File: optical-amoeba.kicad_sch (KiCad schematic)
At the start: 5 parts, among them J1 Conn_01x08_Male, Q1 Q_Photo_NPN_CE

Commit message: Added PCB for full keyboard
 M .gitignore
A  OpticalSymbols_Library.kicad_sym
A  Optical_Parts.pretty/BlackPill_STLINK.kicad_mod
M  Optical_Parts.pretty/Everlight_IR_IR12-21C_TR8.kicad_mod
M  Optical_Parts.pretty/Everlight_PT_PT12-21C_TR8.kicad_mod
M  Optical_Parts.pretty/Gateron_Optical_Switch.kicad_mod
A  Optical_Parts.pretty/Gateron_Switch_Basic.kicad_mod
A  Optical_Parts.pretty/Switch_Cutout.kicad_mod
A  Optical_Parts.pretty/Switch_Cutout_1.25u.kicad_mod
A  Optical_Parts.pretty/Switch_Cutout_1.5u.kicad_mod
A  Optical_Parts.pretty/Switch_Cutout_1.75u.kicad_mod
M  README.md
A  keyboard-pcb/.gitignore
A  keyboard-pcb/fp-lib-table
A  keyboard-pcb/keyboard-pcb.kicad_pcb
A  keyboard-pcb/keyboard-pcb.kicad_prl
A  keyboard-pcb/keyboard-pcb.kicad_pro
A  keyboard-pcb/keyboard-pcb.kicad_sch
A  keyboard-pcb/placefp.py
A  keyboard-pcb/switch.kicad_sch
A  keyboard-pcb/sym-lib-table
M  optical-amoeba.kicad_pcb
M  optical-amoeba.kicad_sch
A  switch-cutout/.gitignore
A  switch-cutout/fp-lib-table
A  switch-cutout/switch-cutout.kicad_pcb
A  switch-cutout/switch-cutout.kicad_prl
A  switch-cutout/switch-cutout.kicad_pro
A  switch-cutout/switch-cutout.kicad_sch
A  sym-lib-table
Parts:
- Q1: footprint Optical_Parts:Everlight_PT_PT12-21B_TR8 -> Optical_Parts:Everlight_PT_PT12-21C_TR8
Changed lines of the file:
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@@
       (effects (font (size 1.27 1.27)) (justify left))
     )
-    (property "Footprint" "Optical_Parts:Everlight_PT_PT12-21B_TR8" (id 2) (at 125.73 80.01 0)
+    (property "Footprint" "Optical_Parts:Everlight_PT_PT12-21C_TR8" (id 2) (at 125.73 80.01 0)
       (effects (font (size 1.27 1.27)) hide)
     )
@@
     )
     (path "/548bb468-a13e-41e7-a6b9-f73eb3b9ea63"
-      (reference "Q1") (unit 1) (value "Q_Photo_NPN_CE") (footprint "Optical_Parts:Everlight_PT_PT12-21B_TR8")
+      (reference "Q1") (unit 1) (value "Q_Photo_NPN_CE") (footprint "Optical_Parts:Everlight_PT_PT12-21C_TR8")
     )
     (path "/23503685-6c48-4b6b-a5a1-d4b81440ce50"

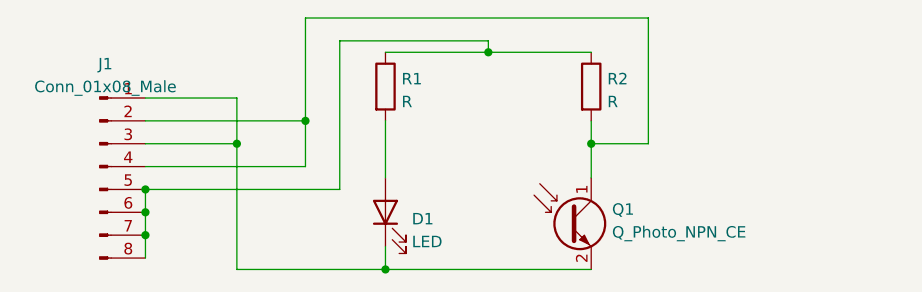
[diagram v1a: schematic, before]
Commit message: Added footprints
M  Optical_Parts.pretty/BlackPill_STLINK.kicad_mod
M  Optical_Parts.pretty/BlackPill_STLINK2.kicad_mod
M  Optical_Parts.pretty/Everlight_IR_IR12-21C_TR8.kicad_mod
M  Optical_Parts.pretty/Everlight_PT_PT12-21C_TR8.kicad_mod
M  Optical_Parts.pretty/Gateron_Optical_Switch.kicad_mod
M  Optical_Parts.pretty/MountingHole_2.2mm_M2_jlcpcb.kicad_mod
M  Optical_Parts.pretty/Switch_Cutout.kicad_mod
M  Optical_Parts.pretty/Switch_Cutout_1.25u.kicad_mod
M  Optical_Parts.pretty/Switch_Cutout_1.5u.kicad_mod
M  Optical_Parts.pretty/Switch_Cutout_1.75u.kicad_mod
M  README.md
M  optical-amoeba.kicad_pcb
M  optical-amoeba.kicad_prl
M  optical-amoeba.kicad_sch
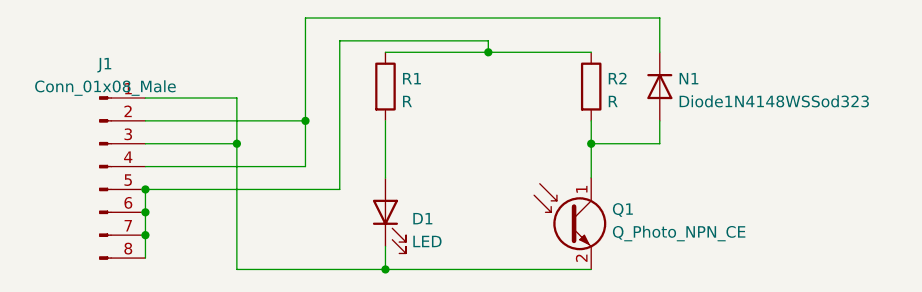
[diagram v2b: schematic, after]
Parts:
- added N1: Diode1N4148WSSod323, Diode_SMD:D_SOD-323, symbol OpticalSymbols_Library:Diode1N4148WSSod323
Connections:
- net at J1.2 (Pin_2), J1.4 (Pin_4): now also N1.1 (K); no longer Q1.1 (C), R2.2
- new net: N1.2 (A), Q1.1 (C), R2.2
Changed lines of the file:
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@@
   (junction (at 91.44 71.12) (diameter 0) (color 0 0 0 0)
   )
+  (wire (pts (xy 130.81 73.66) (xy 130.81 71.12))
+    (stroke (width 0) (type default) (color 0 0 0 0))
+  )
   (wire (pts (xy 111.76 63.5) (xy 123.19 63.5))
     (stroke (width 0) (type default) (color 0 0 0 0))
@@
     (stroke (width 0) (type default) (color 0 0 0 0))
   )
-  (wire (pts (xy 129.54 73.66) (xy 123.19 73.66))
+  (wire (pts (xy 123.19 73.66) (xy 130.81 73.66))
     (stroke (width 0) (type default) (color 0 0 0 0))
   )
@@
     (stroke (width 0) (type default) (color 0 0 0 0))
   )
-  (wire (pts (xy 129.54 59.69) (xy 129.54 73.66))
-    (stroke (width 0) (type default) (color 0 0 0 0))
-  )
   (wire (pts (xy 95.25 78.74) (xy 95.25 62.23))
     (stroke (width 0) (type default) (color 0 0 0 0))
@@
     (stroke (width 0) (type default) (color 0 0 0 0))
   )
-  (wire (pts (xy 91.44 59.69) (xy 129.54 59.69))
+  (wire (pts (xy 91.44 59.69) (xy 130.81 59.69))
     (stroke (width 0) (type default) (color 0 0 0 0))
   )
@@
   )
   (wire (pts (xy 73.66 71.12) (xy 91.44 71.12))
+    (stroke (width 0) (type default) (color 0 0 0 0))
+  )
+  (wire (pts (xy 130.81 63.5) (xy 130.81 59.69))
     (stroke (width 0) (type default) (color 0 0 0 0))
   )
@@
     (pin "2")
   )
+  (symbol (lib_id "OpticalSymbols_Library:Diode1N4148WSSod323") (at 130.81 67.31 270) (unit 1)
+    (in_bom yes) (on_board yes) (fields_autoplaced)
+    (property "Reference" "N1" (id 0) (at 132.842 66.4753 90)
+      (effects (font (size 1.27 1.27)) (justify left))
+    )
+    (property "Value" "Diode1N4148WSSod323" (id 1) (at 132.842 69.0122 90)
+      (effects (font (size 1.27 1.27)) (justify left))
+    )
+    (property "Footprint" "Diode_SMD:D_SOD-323" (id 2) (at 126.365 67.31 0)
+      (effects (font (size 1.27 1.27)) hide)
+    )
+    (property "Datasheet" "https://www.vishay.com/docs/85751/1n4148ws.pdf" (id 3) (at 130.81 67.31 0)
+      (effects (font (size 1.27 1.27)) hide)
+    )
+    (property "LCSC" "C2128" (id 4) (at 130.81 67.31 0)
+      (effects (font (size 1.27 1.27)) hide)
+    )
+    (property "JLC" "SOD-323" (id 5) (at 130.81 67.31 0)
+      (effects (font (size 1.27 1.27)) hide)
+    )
+    (pin "1")
+    (pin "2")
+  )
   (symbol (lib_id "Device:Q_Photo_NPN_CE") (at 120.65 82.55 0) (unit 1)
     (in_bom yes) (on_board yes) (fields_autoplaced)
@@
       (reference "J1") (unit 1) (value "Conn_01x08_Male") (footprint "Optical_Parts:Gateron_Optical_Switch")
     )
+    (path "/3d23fdea-f6ec-4963-8317-c51d7bf80624"
+      (reference "N1") (unit 1) (value "Diode1N4148WSSod323") (footprint "Diode_SMD:D_SOD-323")
+    )
     (path "/548bb468-a13e-41e7-a6b9-f73eb3b9ea63"

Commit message: Separated power sourcde for PT and Led
Having same power source necessiates a diode; Diode degrades
performance at read pin

M  OpticalSymbols_Library.kicad_sym
M  Optical_Parts.pretty/Gateron_Optical_Switch.kicad_mod
M  optical-amoeba.kicad_pcb
M  optical-amoeba.kicad_prl
M  optical-amoeba.kicad_sch
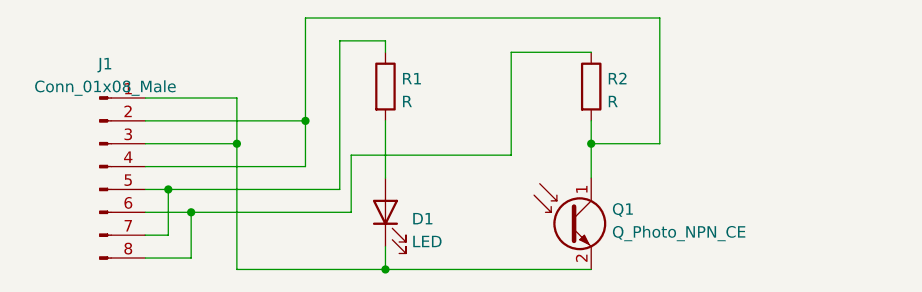
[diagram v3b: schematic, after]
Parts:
- removed N1: Diode1N4148WSSod323, Diode_SMD:D_SOD-323, symbol OpticalSymbols_Library:Diode1N4148WSSod323
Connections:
- net at J1.2 (Pin_2), J1.4 (Pin_4): now also Q1.1 (C), R2.2
- net at J1.5 (Pin_5), J1.7 (Pin_7), R1.1: no longer J1.6 (Pin_6), J1.8 (Pin_8), R2.1
- new net: J1.6 (Pin_6), J1.8 (Pin_8), R2.1
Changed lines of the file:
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@@
   (junction (at 83.82 73.66) (diameter 0) (color 0 0 0 0)
   )
-  (junction (at 73.66 78.74) (diameter 0) (color 0 0 0 0)
-  )
-  (junction (at 73.66 83.82) (diameter 0) (color 0 0 0 0)
+  (junction (at 76.2 78.74) (diameter 0) (color 0 0 0 0)
   )
   (junction (at 100.33 87.63) (diameter 0) (color 0 0 0 0)
@@
   (junction (at 123.19 73.66) (diameter 0) (color 0 0 0 0)
   )
-  (junction (at 73.66 81.28) (diameter 0) (color 0 0 0 0)
-  )
-  (junction (at 111.76 63.5) (diameter 0) (color 0 0 0 0)
-  )
   (junction (at 91.44 71.12) (diameter 0) (color 0 0 0 0)
   )
-  (wire (pts (xy 130.81 73.66) (xy 130.81 71.12))
-    (stroke (width 0) (type default) (color 0 0 0 0))
-  )
-  (wire (pts (xy 111.76 63.5) (xy 123.19 63.5))
+  (junction (at 78.74 81.28) (diameter 0) (color 0 0 0 0)
+  )
+  (wire (pts (xy 100.33 62.23) (xy 95.25 62.23))
+    (stroke (width 0) (type default) (color 0 0 0 0))
+  )
+  (wire (pts (xy 96.52 74.93) (xy 96.52 81.28))
     (stroke (width 0) (type default) (color 0 0 0 0))
   )
@@
     (stroke (width 0) (type default) (color 0 0 0 0))
   )
-  (wire (pts (xy 95.25 62.23) (xy 111.76 62.23))
+  (wire (pts (xy 114.3 74.93) (xy 96.52 74.93))
+    (stroke (width 0) (type default) (color 0 0 0 0))
+  )
+  (wire (pts (xy 114.3 63.5) (xy 114.3 74.93))
+    (stroke (width 0) (type default) (color 0 0 0 0))
+  )
+  (wire (pts (xy 73.66 83.82) (xy 76.2 83.82))
     (stroke (width 0) (type default) (color 0 0 0 0))
   )
@@
     (stroke (width 0) (type default) (color 0 0 0 0))
   )
+  (wire (pts (xy 76.2 83.82) (xy 76.2 78.74))
+    (stroke (width 0) (type default) (color 0 0 0 0))
+  )
   (wire (pts (xy 91.44 71.12) (xy 91.44 59.69))
     (stroke (width 0) (type default) (color 0 0 0 0))
   )
+  (wire (pts (xy 73.66 86.36) (xy 78.74 86.36))
+    (stroke (width 0) (type default) (color 0 0 0 0))
+  )
   (wire (pts (xy 123.19 71.12) (xy 123.19 73.66))
     (stroke (width 0) (type default) (color 0 0 0 0))
   )
-  (wire (pts (xy 73.66 78.74) (xy 95.25 78.74))
-    (stroke (width 0) (type default) (color 0 0 0 0))
-  )
-  (wire (pts (xy 111.76 62.23) (xy 111.76 63.5))
+  (wire (pts (xy 73.66 78.74) (xy 76.2 78.74))
+    (stroke (width 0) (type default) (color 0 0 0 0))
+  )
+  (wire (pts (xy 78.74 81.28) (xy 78.74 86.36))
     (stroke (width 0) (type default) (color 0 0 0 0))
   )
@@
     (stroke (width 0) (type default) (color 0 0 0 0))
   )
-  (wire (pts (xy 73.66 81.28) (xy 73.66 83.82))
-    (stroke (width 0) (type default) (color 0 0 0 0))
-  )
   (wire (pts (xy 100.33 87.63) (xy 123.19 87.63))
     (stroke (width 0) (type default) (color 0 0 0 0))
   )
-  (wire (pts (xy 73.66 83.82) (xy 73.66 86.36))
-    (stroke (width 0) (type default) (color 0 0 0 0))
-  )
   (wire (pts (xy 83.82 87.63) (xy 100.33 87.63))
     (stroke (width 0) (type default) (color 0 0 0 0))
@@
     (stroke (width 0) (type default) (color 0 0 0 0))
   )
+  (wire (pts (xy 123.19 63.5) (xy 114.3 63.5))
+    (stroke (width 0) (type default) (color 0 0 0 0))
+  )
+  (wire (pts (xy 78.74 81.28) (xy 96.52 81.28))
+    (stroke (width 0) (type default) (color 0 0 0 0))
+  )
   (wire (pts (xy 100.33 85.09) (xy 100.33 87.63))
     (stroke (width 0) (type default) (color 0 0 0 0))
@@
     (stroke (width 0) (type default) (color 0 0 0 0))
   )
-  (wire (pts (xy 130.81 63.5) (xy 130.81 59.69))
-    (stroke (width 0) (type default) (color 0 0 0 0))
-  )
-  (wire (pts (xy 73.66 78.74) (xy 73.66 81.28))
+  (wire (pts (xy 100.33 63.5) (xy 100.33 62.23))
+    (stroke (width 0) (type default) (color 0 0 0 0))
+  )
+  (wire (pts (xy 130.81 59.69) (xy 130.81 73.66))
+    (stroke (width 0) (type default) (color 0 0 0 0))
+  )
+  (wire (pts (xy 73.66 81.28) (xy 78.74 81.28))
     (stroke (width 0) (type default) (color 0 0 0 0))
   )
@@
     (stroke (width 0) (type default) (color 0 0 0 0))
   )
-  (wire (pts (xy 100.33 63.5) (xy 111.76 63.5))
+  (wire (pts (xy 76.2 78.74) (xy 95.25 78.74))
     (stroke (width 0) (type default) (color 0 0 0 0))
   )
@@
     (pin "2")
   )
-  (symbol (lib_id "OpticalSymbols_Library:Diode1N4148WSSod323") (at 130.81 67.31 270) (unit 1)
-    (in_bom yes) (on_board yes) (fields_autoplaced)
-    (property "Reference" "N1" (id 0) (at 132.842 66.4753 90)
-      (effects (font (size 1.27 1.27)) (justify left))
-    )
-    (property "Value" "Diode1N4148WSSod323" (id 1) (at 132.842 69.0122 90)
-      (effects (font (size 1.27 1.27)) (justify left))
-    )
-    (property "Footprint" "Diode_SMD:D_SOD-323" (id 2) (at 126.365 67.31 0)
-      (effects (font (size 1.27 1.27)) hide)
-    )
-    (property "Datasheet" "https://www.vishay.com/docs/85751/1n4148ws.pdf" (id 3) (at 130.81 67.31 0)
-      (effects (font (size 1.27 1.27)) hide)
-    )
-    (property "LCSC" "C2128" (id 4) (at 130.81 67.31 0)
-      (effects (font (size 1.27 1.27)) hide)
-    )
-    (property "JLC" "SOD-323" (id 5) (at 130.81 67.31 0)
-      (effects (font (size 1.27 1.27)) hide)
-    )
-    (pin "1")
-    (pin "2")
-  )
   (symbol (lib_id "Device:Q_Photo_NPN_CE") (at 120.65 82.55 0) (unit 1)
     (in_bom yes) (on_board yes) (fields_autoplaced)
@@
       (reference "J1") (unit 1) (value "Conn_01x08_Male") (footprint "Optical_Parts:Gateron_Optical_Switch")
     )
-    (path "/3d23fdea-f6ec-4963-8317-c51d7bf80624"
-      (reference "N1") (unit 1) (value "Diode1N4148WSSod323") (footprint "Diode_SMD:D_SOD-323")
-    )
     (path "/548bb468-a13e-41e7-a6b9-f73eb3b9ea63"

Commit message: Add jlcpcb gerber and assembly files
M  OpticalSymbols_Library.kicad_sym
A  jlcpcb/gerber/optical-amoeba-B_Cu.gbl
A  jlcpcb/gerber/optical-amoeba-B_Mask.gbs
A  jlcpcb/gerber/optical-amoeba-B_Paste.gbp
A  jlcpcb/gerber/optical-amoeba-B_Silkscreen.gbo
A  jlcpcb/gerber/optical-amoeba-Edge_Cuts.gm1
A  jlcpcb/gerber/optical-amoeba-F_Cu.gtl
A  jlcpcb/gerber/optical-amoeba-F_Mask.gts
A  jlcpcb/gerber/optical-amoeba-F_Paste.gtp
A  jlcpcb/gerber/optical-amoeba-F_Silkscreen.gto
A  jlcpcb/gerber/optical-amoeba-NPTH-drl_map.gbr
A  jlcpcb/gerber/optical-amoeba-NPTH.drl
A  jlcpcb/gerber/optical-amoeba-PTH-drl_map.gbr
A  jlcpcb/gerber/optical-amoeba-PTH.drl
M  optical-amoeba.kicad_pcb
M  optical-amoeba.kicad_prl
M  optical-amoeba.kicad_sch
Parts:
- removed R1: R, Resistor_SMD:R_0603_1608Metric, symbol Device:R
- removed R2: R, Resistor_SMD:R_0805_2012Metric, symbol Device:R
- added RL1: R_Led, Resistor_SMD:R_0603_1608Metric, symbol OpticalSymbols_Library:R_Led
- added RP1: R_PT, Resistor_SMD:R_0805_2012Metric, symbol OpticalSymbols_Library:R_PT
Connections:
- net at J1.2 (Pin_2), J1.4 (Pin_4), Q1.1 (C): now also RP1.2
- net at J1.5 (Pin_5), J1.7 (Pin_7): now also RL1.1
- net at J1.6 (Pin_6), J1.8 (Pin_8): now also RP1.1
- net at D1.2 (A): now also RL1.2
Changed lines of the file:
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@@
     (pin "8")
-  )
-  (symbol (lib_id "Device:R") (at 100.33 67.31 0) (unit 1)
-    (in_bom yes) (on_board yes) (fields_autoplaced)
-    (property "Reference" "R1" (id 0) (at 102.108 66.4753 0)
-      (effects (font (size 1.27 1.27)) (justify left))
-    )
-    (property "Value" "R" (id 1) (at 102.108 69.0122 0)
-      (effects (font (size 1.27 1.27)) (justify left))
-    )
-    (property "Footprint" "Resistor_SMD:R_0603_1608Metric" (id 2) (at 98.552 67.31 90)
-      (effects (font (size 1.27 1.27)) hide)
-    )
-    (property "Datasheet" "~" (id 3) (at 100.33 67.31 0)
-      (effects (font (size 1.27 1.27)) hide)
-    )
-    (property "JLC" "0603" (id 4) (at 100.33 67.31 0)
-      (effects (font (size 1.27 1.27)) hide)
-    )
-    (property "LCSC" "C4190" (id 5) (at 100.33 67.31 0)
-      (effects (font (size 1.27 1.27)) hide)
-    )
-    (pin "1")
-    (pin "2")
   )
   (symbol (lib_id "Device:Q_Photo_NPN_CE") (at 120.65 82.55 0) (unit 1)
@@
     (property "LCSC" "C264383" (id 5) (at 120.65 82.55 0)
       (effects (font (size 1.27 1.27)) hide)
+    )
+    (pin "1")
+    (pin "2")
+  )
+  (symbol (lib_id "OpticalSymbols_Library:R_PT") (at 123.19 67.31 0) (unit 1)
+    (in_bom yes) (on_board yes) (fields_autoplaced)
+    (property "Reference" "RP1" (id 0) (at 124.968 66.4753 0)
+      (effects (font (size 1.27 1.27)) (justify left))
+    )
+    (property "Value" "R_PT" (id 1) (at 124.968 69.0122 0)
+      (effects (font (size 1.27 1.27)) (justify left))
+    )
+    (property "Footprint" "Resistor_SMD:R_0805_2012Metric" (id 2) (at 124.46 73.66 90)
+      (effects (font (size 1.27 1.27)) (justify left) hide)
+    )
+    (property "Datasheet" "~" (id 3) (at 123.19 68.58 0)
+      (effects (font (size 1.27 1.27)) hide)
+    )
+    (property "JLC" "0805-2012" (id 4) (at 120.65 71.12 0)
+      (effects (font (size 0.5 0.5)) hide)
+    )
+    (property "LCSC" "C17713" (id 5) (at 127 63.5 0)
+      (effects (font (size 0.5 0.5)) hide)
+    )
+    (pin "1")
+    (pin "2")
+  )
+  (symbol (lib_id "OpticalSymbols_Library:R_Led") (at 100.33 67.31 0) (unit 1)
+    (in_bom yes) (on_board yes) (fields_autoplaced)
+    (property "Reference" "RL1" (id 0) (at 102.108 66.4753 0)
+      (effects (font (size 1.27 1.27)) (justify left))
+    )
+    (property "Value" "R_Led" (id 1) (at 102.108 69.0122 0)
+      (effects (font (size 1.27 1.27)) (justify left))
+    )
+    (property "Footprint" "Resistor_SMD:R_0603_1608Metric" (id 2) (at 101.6 73.66 90)
+      (effects (font (size 1.27 1.27)) (justify left) hide)
+    )
+    (property "Datasheet" "~" (id 3) (at 100.33 68.58 0)
+      (effects (font (size 1.27 1.27)) hide)
+    )
+    (property "JLC" "0603-1608" (id 4) (at 104.14 71.12 0)
+      (effects (font (size 0.5 0.5)) hide)
+    )
+    (property "LCSC" "C4190" (id 5) (at 104.14 63.5 0)
+      (effects (font (size 0.5 0.5)) hide)
     )
     (pin "1")
@@
     (pin "2")
   )
-  (symbol (lib_id "Device:R") (at 123.19 67.31 0) (unit 1)
-    (in_bom yes) (on_board yes) (fields_autoplaced)
-    (property "Reference" "R2" (id 0) (at 124.968 66.4753 0)
-      (effects (font (size 1.27 1.27)) (justify left))
-    )
-    (property "Value" "R" (id 1) (at 124.968 69.0122 0)
-      (effects (font (size 1.27 1.27)) (justify left))
-    )
-    (property "Footprint" "Resistor_SMD:R_0805_2012Metric" (id 2) (at 121.412 67.31 90)
-      (effects (font (size 1.27 1.27)) hide)
-    )
-    (property "Datasheet" "~" (id 3) (at 123.19 67.31 0)
-      (effects (font (size 1.27 1.27)) hide)
-    )
-    (property "JLC" "0805" (id 4) (at 123.19 67.31 0)
-      (effects (font (size 1.27 1.27)) hide)
-    )
-    (property "LCSC" "C17713" (id 5) (at 123.19 67.31 0)
-      (effects (font (size 1.27 1.27)) hide)
-    )
-    (pin "1")
-    (pin "2")
-  )
   (sheet_instances
     (path "/" (page "1"))
@@
       (reference "Q1") (unit 1) (value "Q_Photo_NPN_CE") (footprint "Optical_Parts:Everlight_PT_PT12-21C_TR8")
     )
-    (path "/23503685-6c48-4b6b-a5a1-d4b81440ce50"
-      (reference "R1") (unit 1) (value "R") (footprint "Resistor_SMD:R_0603_1608Metric")
+    (path "/ae276f22-adb9-4929-9ca1-9c2610beeee5"
+      (reference "RL1") (unit 1) (value "R_Led") (footprint "Resistor_SMD:R_0603_1608Metric")
     )
-    (path "/f10b485f-7f48-45c9-945a-aa2d898f983c"
-      (reference "R2") (unit 1) (value "R") (footprint "Resistor_SMD:R_0805_2012Metric")
+    (path "/5a77a3a7-0cd1-4017-977f-0774e58d08ed"
+      (reference "RP1") (unit 1) (value "R_PT") (footprint "Resistor_SMD:R_0805_2012Metric")
     )
   )
